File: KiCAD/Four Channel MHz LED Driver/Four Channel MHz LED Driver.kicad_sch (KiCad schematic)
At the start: 96 parts, among them J1 Barrel_Jack_Switch, J10 Conn_01x24_Female, J2 Conn_01x02_Female, J3 8P8C_Shielded_x4, J4 Conn_01x03_Male, J5 Conn_01x03_Female, J6 Conn_01x08_Female, J7 Conn_01x03_Female, J8 Conn_01x05_Female, J9 Conn_01x24_Female, M1 Fan_4pin, Q1 SUM70060E, SW1 Pushbutton_with_LED, SW2 Pushbutton_with_LED, SW3 Pushbutton_with_LED, SW4 Pushbutton_with_LED, SW5 SW_SPDT, U1 12V boost, U10 Teensy4.1, U13 EL7457CSZ-T7, U2 SN74LV4T125PWR, U3 DPBW06F-05, U4 TMUX1204DGSR, U5 BDJ0GA5WEFJ-E2, U6 ADP7182AUJZ-1.8-R7, U7 LT6200CS8-10, U8 IRF9358TRPBF, U9 IRF9358TRPBF

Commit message: update
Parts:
- added C23: 2.2uF, Custom Footprints:0508_Capacitor, symbol Device:C_Small
- added JP7, JP8: Jumper_NC_Small, Resistor_SMD:R_1206_3216Metric, symbol Four Channel MHz LED Driver-rescue:Jumper_NC_Small-Device
- added U12: DAC80501ZDGSR, Custom Footprints:DGS10_TEX, symbol Custom_parts:DAC80501ZDGSR
- JP4: footprint Custom Footprints:20A_shunt_5104 -> Resistor_SMD:R_1206_3216Metric; Part # 5104 -> 5108
- U10: footprint Custom Footprints:Teensy_3_6_with_headers -> Custom Footprints:Teensy_4_1_with_headers
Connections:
- net 3.3V: now also D1.5, J10.~, U10.36 (14_A0_TX3_SPDIF_OUT), U10.46 (3V3), U10.7 (5_IN2), U10.8 (6_OUT1D), C23.2, U12.1 (VDD); no longer JP4.2
- net A-D_input_1: now also U10.32 (40_A16); no longer U10.33 (41_A17)
- net A-D_input_2: now also U10.31 (39_MISO1_OUT1A); no longer U10.32 (40_A16)
- net A-D_input_3: now also U10.29 (37_CS); no longer U10.31 (39_MISO1_OUT1A)
- net A-D_input_4: now also U10.28 (36_CS); no longer U10.30 (38_CS1_IN1)
- net Analog_select: now also U10.9 (7_RX2_OUT1A); no longer U10.7 (5_IN2)
- net CS: now also U12.7 (*SYNC/A0)
- net External_thermistor: now also U10.38 (16_A2_RX4_SCL1); no longer U10.42 (20_A6_TX5_LRCLK1)
- net GND: now also C23.1, U12.4 (AGND), U12.5 (SPI2C)
- net Isense_internal: now also U10.39 (17_A3_TX4_SDA1); no longer U10.43 (21_A7_RX5_BCLK1)
- net LED_pot: now also U10.30 (38_CS1_IN1); no longer U10.25 (33_MCLK2)
- net MOSFET_temp: now also JP4.1, JP4.2
- net MOSI: now also U12.8 (SDIN/SDA)
- net Over_temp_alarm2: now also U10.11 (9_OUT1C); no longer U10.10 (8_TX2_IN1)
- net Resistor_temp: now also U10.33 (41_A17), JP8.1, JP8.2; no longer U10.36 (14_A0_TX3_SPDIF_OUT)
- net SCK: now also U12.6 (SCLK/SCL)
- net Toggle_switch: now also U10.10 (8_TX2_IN1); no longer U10.11 (9_OUT1C)
- net internal_analog: now also JP7.1
- removed net External_5V_PWM2: J10.~, U10.40 (18_A4_SDA), U2.2 (1A)
- removed net External_5V_PWM3: J10.~, U10.41 (19_A5_SCL), U2.5 (2A)
- removed net SCL0: J10.~, J3.17, U10.38 (16_A2_RX4_SCL1)
- removed net SDA0: J10.~, J3.19, U10.39 (17_A3_TX4_SDA1)
- new net: J10.~, U10.25 (33_MCLK2)
- new net: JP7.2, U12.2 (VOUT)
- new net A-D_input_5: J10.~, J3.17, U10.41 (19_A5_SCL)
- new net A-D_input_6: J10.~, J3.19, U10.40 (18_A4_SDA)
- new net External_5V_2: J10.~, U10.43 (21_A7_RX5_BCLK1), U2.2 (1A)
- new net External_5V_3: J10.~, U10.42 (20_A6_TX5_LRCLK1), U2.5 (2A)
- no-connect marks 12 -> 13
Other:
- note removed: "-------ADC0------"
- note removed: "--ADC1--"
- note removed: "ADC0"
- note removed: "ADC1"
- note removed: "https://forum.pjrc.com/attachment.php?attachmentid=10666&d=1495536536"

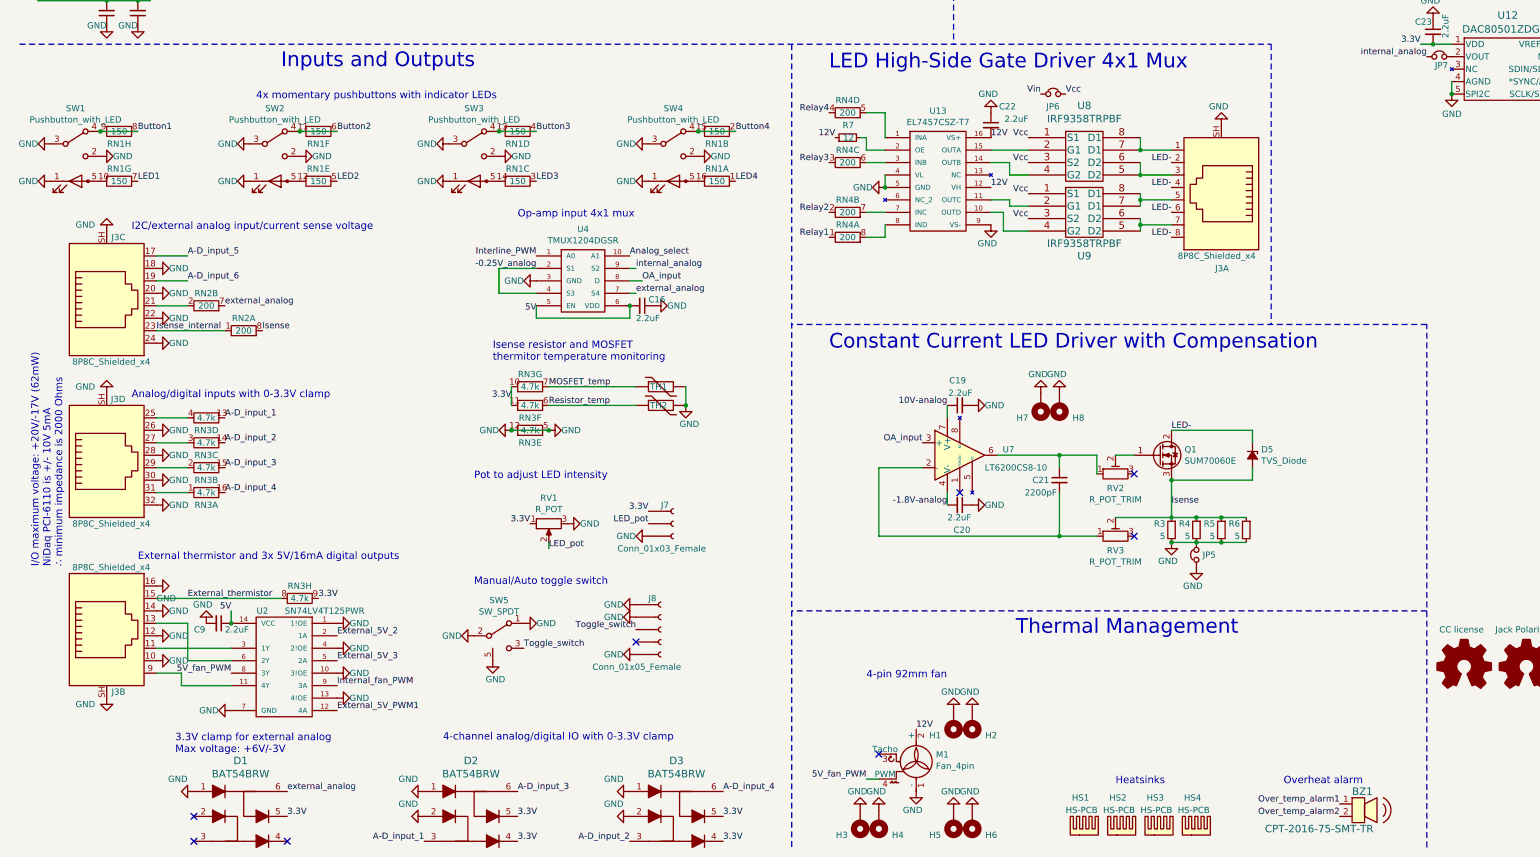
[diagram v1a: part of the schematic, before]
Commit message: Working draft all connected
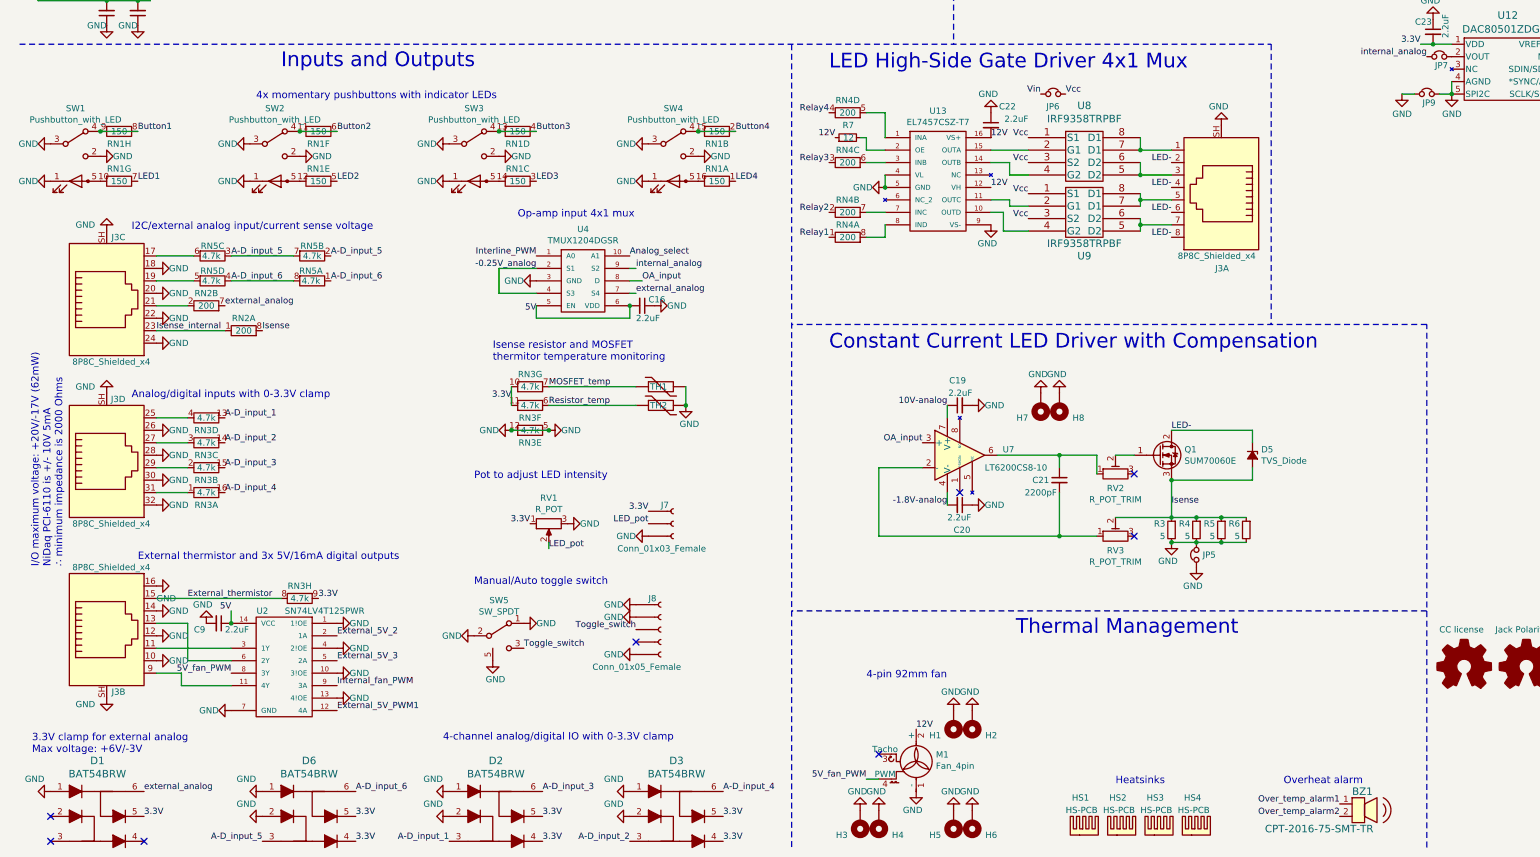
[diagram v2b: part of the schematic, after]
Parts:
- added D6: BAT54BRW, Package_TO_SOT_SMD:SOT-363_SC-70-6, symbol Custom_parts:BAT54BRW
- added JP9: Jumper_NC_Small, Resistor_SMD:R_1206_3216Metric, symbol Four Channel MHz LED Driver-rescue:Jumper_NC_Small-Device
- added RN5: 4.7k, Custom Footprints:RESCAXS127P508X320X70-8N, symbol Device:R_Pack04_Split
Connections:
- net 3.3V: now also D6.4, D6.5
- net A-D_input_5: now also D6.3, RN5.2 (R2.1), RN5.3 (R3.1), RN5.7 (R2.2); no longer J3.17
- net A-D_input_6: now also D6.6, RN5.1 (R1.1), RN5.4 (R4.1), RN5.8 (R1.2); no longer J3.19
- net GND: now also D6.1, D6.2, JP9.1, JP9.2
- new net: J3.17, RN5.6 (R3.2)
- new net: J3.19, RN5.5 (R4.2)
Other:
- moved on the sheet: D1, D2

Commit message: minor tweaks
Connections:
- net 3.3V: no longer U10.7 (5_IN2)
- net NC4: now reaches J10.~, U10.25 (33_MCLK2)
- net NC3: now reaches J10.~, U10.26 (34_RX8)
- net NC2: now reaches J10.~, U10.27 (35_TX8)
- new net NC1: J9.~, U10.7 (5_IN2)
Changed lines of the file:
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@@
+		)
+	)
+	(label "NC3"
+		(at 341.63 90.17 0)
+		(fields_autoplaced yes)
+		(effects
+			(font
+				(size 1.27 1.27)
+			)
+			(justify left bottom)
 		)
 	)
@@
 		)
 	)
-	(label "3.3V"
-		(at 293.37 52.07 180)
-		(fields_autoplaced yes)
-		(effects
-			(font
-				(size 1.27 1.27)
-			)
-			(justify right bottom)
-		)
-	)
 	(label "Vin"
 		(at 16.51 69.85 180)
@@
 		)
 	)
+	(label "NC4"
+		(at 341.63 92.71 0)
+		(fields_autoplaced yes)
+		(effects
+			(font
+				(size 1.27 1.27)
+			)
+			(justify left bottom)
+		)
+	)
 	(label "A-D_input_6"
 		(at 76.2 168.91 0)
@@
 		)
 	)
+	(label "NC1"
+		(at 293.37 49.53 180)
+		(fields_autoplaced yes)
+		(effects
+			(font
+				(size 1.27 1.27)
+			)
+			(justify right bottom)
+		)
+	)
 	(label "Interline_PWM"
 		(at 118.11 163.83 180)
@@
 	)
 	(label "3.3V"
-		(at 293.37 49.53 180)
-		(fields_autoplaced yes)
-		(effects
-			(font
-				(size 1.27 1.27)
-			)
-			(justify right bottom)
-		)
-	)
+		(at 293.37 52.07 180)
+		(fields_autoplaced yes)
+		(effects
+			(font
+				(size 1.27 1.27)
+			)
+			(justify right bottom)
+		)
+	)
+	(label "NC2"
+		(at 341.63 87.63 0)
+		(fields_autoplaced yes)
+		(effects
+			(font
+				(size 1.27 1.27)
+			)
+			(justify left bottom)
+		)
+	)

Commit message: minor updates
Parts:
- RN5: Manufacturer (none) -> YAGEO; Part (none) -> YC324-JK-074K7L
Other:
- moved on the sheet: C23, JP7, JP9, U12

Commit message: Non-working prototype of getting code switched to 4.1 with external DAC
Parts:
- RN3: Manufacturer CTS Resistor Products -> Panasonic Electronic Components; Part # 742C163472JP -> EXB-2HV472JV
- RN5: Part YC324-JK-074K7L -> (none); Part # (none) -> YC324-JK-074K7L
- U10: Part 1568-DEV-16996-ND -> (none); Part # (none) -> DEV-16996
- U12: Part DAC80501ZDGSR -> (none); Part # (none) -> DAC80501ZDGSR
